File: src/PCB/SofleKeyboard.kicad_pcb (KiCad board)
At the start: 2 copper layers, 132.5 x 101.3 mm, 83 parts, among them J1 LED, J2 4PIN, J3 OLED, SW1 SW_PUSH, SW10 SW_PUSH, SW11 SW_PUSH, SW12 SW_PUSH, SW13 SW_PUSH, SW14 SW_PUSH, SW15 SW_PUSH, SW16 SW_PUSH, SW17 SW_PUSH, SW18 SW_PUSH, SW19 SW_PUSH, SW2 SW_PUSH, SW20 SW_PUSH, SW21 SW_PUSH, SW22 SW_PUSH, SW23 SW_PUSH, SW24 SW_PUSH, SW26 SW_PUSH, SW27 SW_PUSH, SW28 SW_PUSH, SW29 SW_PUSH, SW3 SW_PUSH, SW30 SW_PUSH, SW4 SW_PUSH, SW5 SW_PUSH, SW6 SW_PUSH, SW7 SW_PUSH, SW8 SW_PUSH, SW9 SW_PUSH, U1 ProMicro

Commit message: adding art
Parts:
- added G***: LOGO, art:hand, B.Cu at (156.7, 79.2)
- added G***: LOGO, art:birb, B.Cu at (103.0, 69.8)
- added G***: LOGO, art:birb, F.Cu at (102.8, 69.8)
- added G***: LOGO, art:hand, F.Cu at (160.8, 79.2)
- moved RSW1 0.95 mm to (92.3, 91.8)
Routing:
- net GND: track 104.9 -> 100.4 mm
- net RESET: track 51.2 -> 50.3 mm
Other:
- board text added: "Enoch Chau 2021"

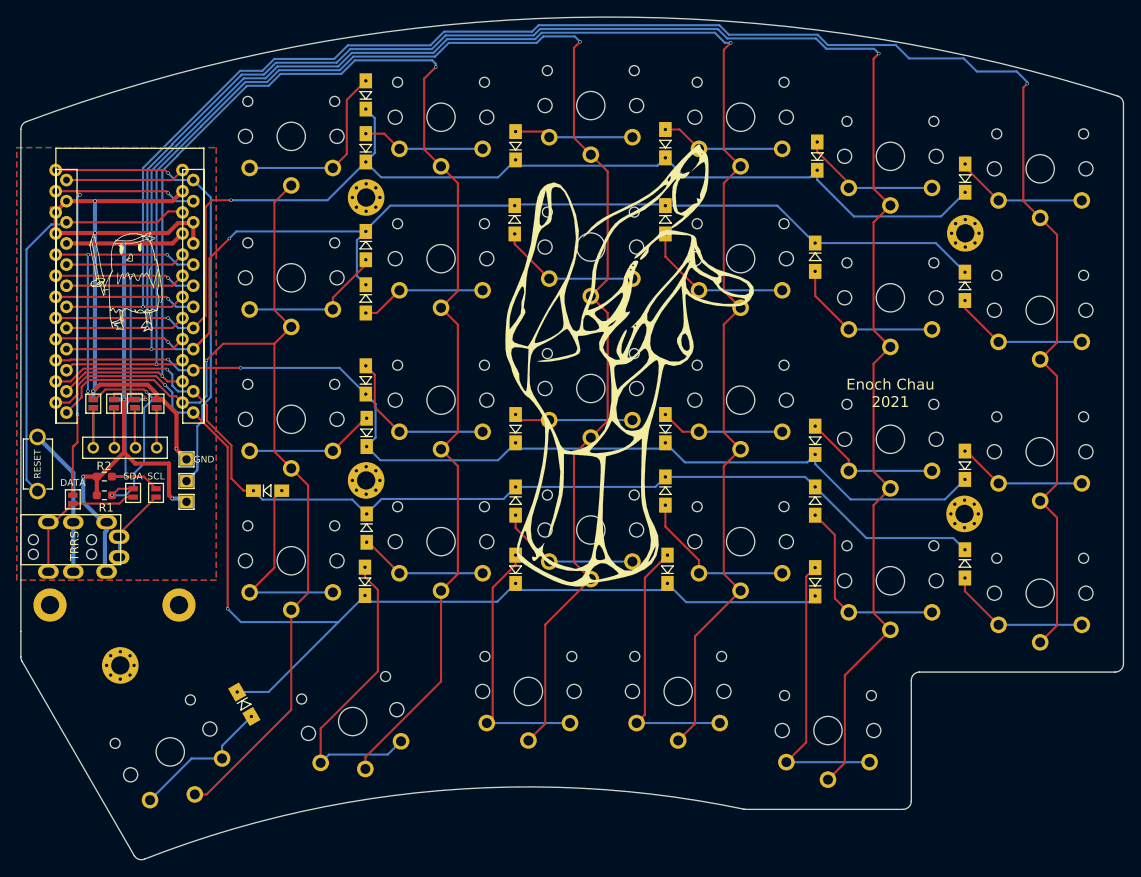
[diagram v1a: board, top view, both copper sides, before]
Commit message: fixing spacing for 1.5u keycap
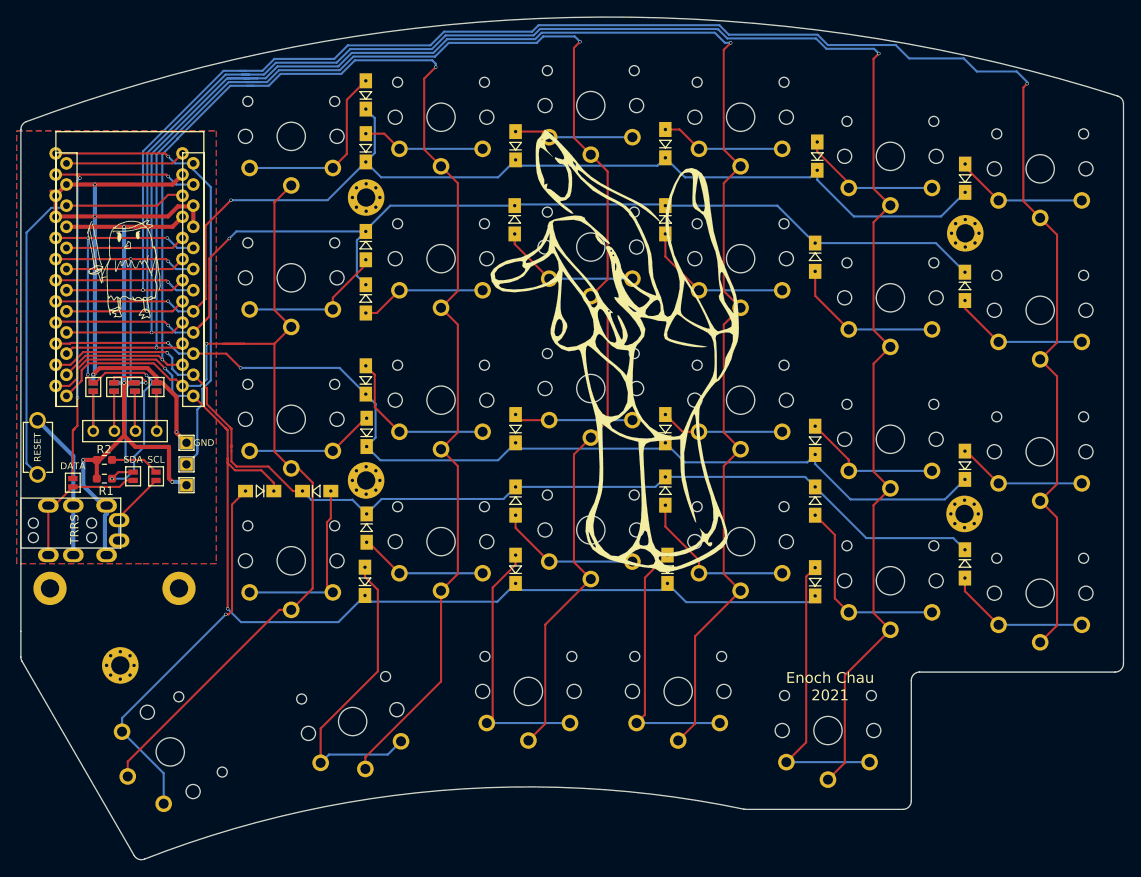
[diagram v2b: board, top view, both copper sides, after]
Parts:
- removed the G*** at (156.7, 79.2)
- removed the G*** at (103.0, 69.8)
- removed the G*** at (102.8, 69.8)
- added G***: LOGO, art:birb, F.Cu at (102.5, 68.2)
- added G***: LOGO, art:hand_right, F.Cu at (164.0, 77.5)
- G***: moved to B.Cu
- moved D26 25.7 mm to (119.0, 95.0), turned to 180 degrees
- moved D19 5.89 mm to (125.8, 95.0)
- moved G*** 3.91 mm to (164.2, 77.5), turned to 180 degrees
- moved DATA 2.00 mm to (96.5, 94.0)
- moved J1 2.00 mm to (110.2, 94.3)
- moved J2 2.00 mm to (90.3, 98.8)
- moved J3 2.00 mm to (99.0, 87.8)
- moved JP1 2.00 mm to (106.6, 82.5)
- moved JP2 2.00 mm to (104.0, 82.5)
- moved JP3 2.00 mm to (101.5, 82.5)
- moved JP4 2.00 mm to (99.0, 82.5)
- moved JP5 2.00 mm to (106.6, 82.5)
- moved JP6 2.00 mm to (104.0, 82.5)
- moved JP7 2.00 mm to (101.5, 82.5)
- moved JP8 2.00 mm to (99.0, 82.5)
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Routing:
- net Net-(D26-Pad2): track 17.2 -> 46.0 mm, vias 0 -> 1
- net row4: track 138.1 -> 132.8 mm
- net col5: track 117.8 -> 121.6 mm
- net col2: track 206.0 -> 209.4 mm
- net row0: track 140.8 -> 137.5 mm
- net row1: track 135.3 -> 133.3 mm
- net row3: track 126.9 -> 128.2 mm
- net Net-(D19-Pad2): track 23.8 -> 22.7 mm
- net row2: track 125.8 -> 126.8 mm
- net col3: track 188.8 -> 189.7 mm

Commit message: adding silks and finalizing design
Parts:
- removed the G*** at (164.0, 77.5)
- removed the G*** at (164.2, 77.5)
- added G***: LOGO, art:hand_dual, F.Cu at (165.5, 76.1)
- moved G*** 1.40 mm to (102.1, 69.6)
- turned SDA to 270 degrees
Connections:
- SDA pad 1: Net-(J2-Pad3) -> SDA
- SDA pad 2: SDA -> Net-(J2-Pad3)
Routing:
- net col5: track 121.6 -> 124.5 mm
- net col0: track 220.7 -> 221.9 mm
- net col1: track 226.2 -> 227.4 mm
- net col3: track 189.7 -> 190.8 mm
- net col2: track 209.4 -> 210.3 mm
- net col4: track 173.6 -> 174.1 mm
